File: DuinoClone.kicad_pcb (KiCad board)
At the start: 2 copper layers, 17 parts, among them J1 Digital pins, J2 Serial, J3 ICSP, J4 I2C, U1 DS1337S+, U2 24LC1025, U3 24LC1025, U4 ATMEGA328P-AU, Y1 Crystal 32MHz, Y2 Crystal 16MHz

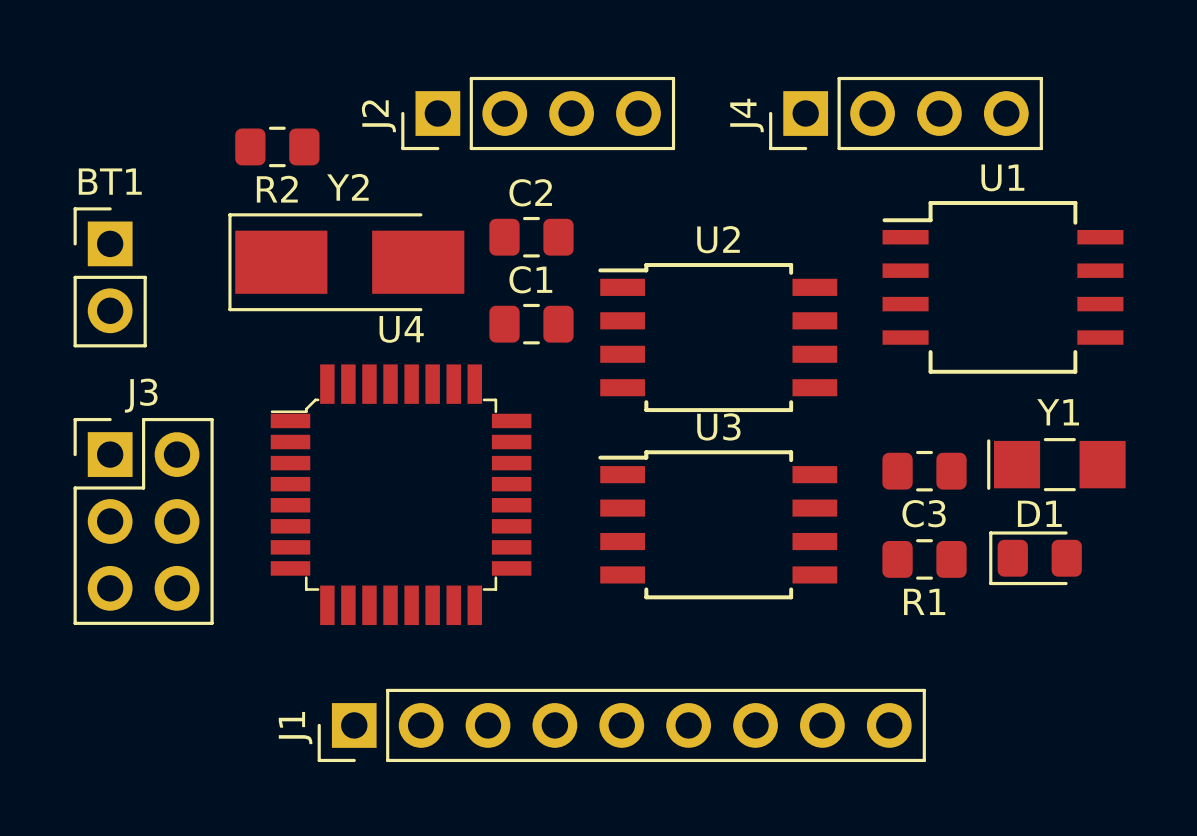
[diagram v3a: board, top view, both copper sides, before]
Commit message: Created PCB outline and drill holes
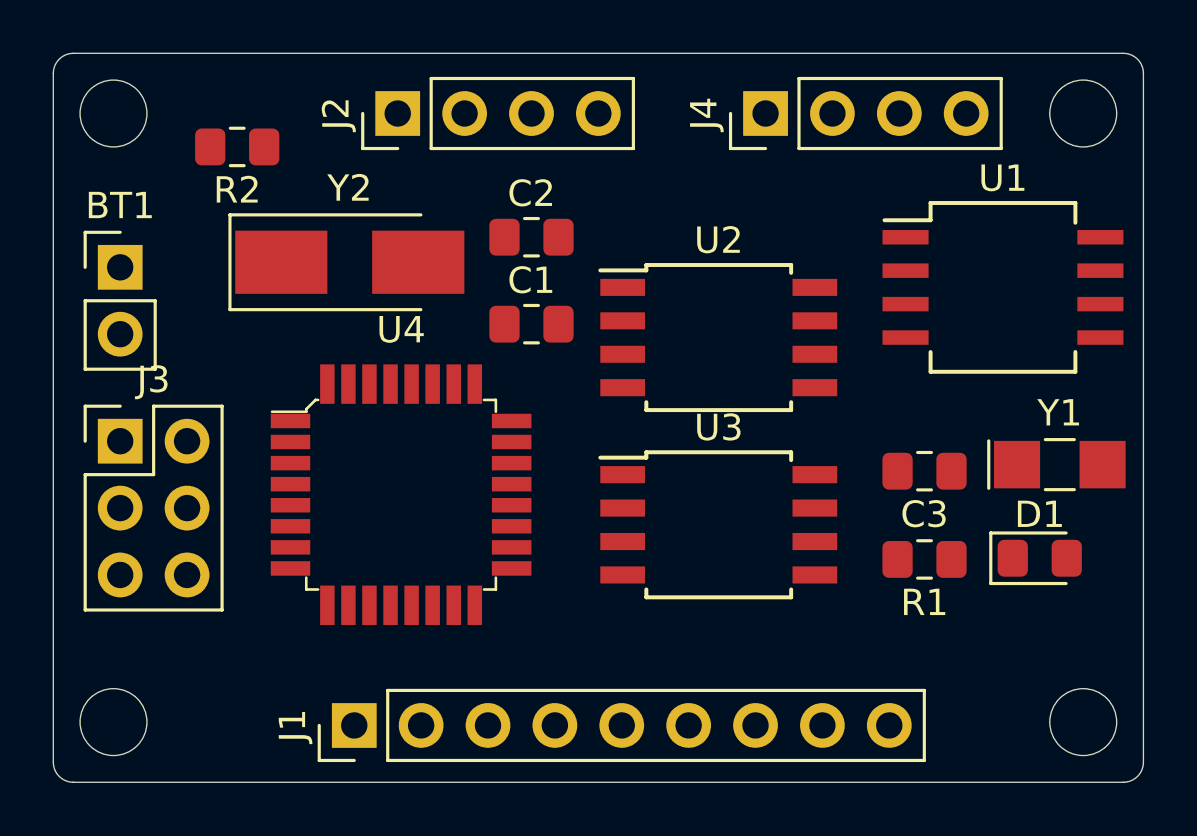
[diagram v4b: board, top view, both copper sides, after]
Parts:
- moved J2 1.52 mm to (93.3, 85.6)
- moved J4 1.52 mm to (107.3, 85.6)
- moved R2 1.52 mm to (87.2, 86.9)
- moved BT1 0.97 mm to (82.8, 91.4)
- moved J3 0.64 mm to (82.8, 98.0)
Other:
- board outline added: 41.4 x 27.7 mm
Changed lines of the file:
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@@
   (general
     (thickness 1.6)
-    (drawings 0)
+    (drawings 12)
     (tracks 0)
     (zones 0)
@@
   )
   (module Connector_PinHeader_2.54mm:PinHeader_1x02_P2.54mm_Vertical (layer F.Cu)
-    (at 82.423 90.551)
+    (at 82.804 91.44)
     (descr "Through hole straight pin header, 1x02, 2.54mm pitch, single row")
     (tags "Through hole pin header THT 1x02 2.54mm single row")
@@
   )
   (module Connector_PinHeader_2.54mm:PinHeader_1x04_P2.54mm_Vertical (layer F.Cu)
-    (at 94.869 85.598 90)
+    (at 93.345 85.598 90)
     (descr "Through hole straight pin header, 1x04, 2.54mm pitch, single row")
     (tags "Through hole pin header THT 1x04 2.54mm single row")
@@
   )
   (module Connector_PinHeader_2.54mm:PinHeader_2x03_P2.54mm_Vertical (layer F.Cu)
-    (at 82.423 98.552)
+    (at 82.804 98.044)
     (descr "Through hole straight pin header, 2x03, 2.54mm pitch, double rows")
     (tags "Through hole pin header THT 2x03 2.54mm double row")
@@
   )
   (module Connector_PinHeader_2.54mm:PinHeader_1x04_P2.54mm_Vertical (layer F.Cu)
-    (at 108.839 85.598 90)
+    (at 107.315 85.598 90)
     (descr "Through hole straight pin header, 1x04, 2.54mm pitch, single row")
     (tags "Through hole pin header THT 1x04 2.54mm single row")
@@
   )
   (module Resistor_SMD:R_0805_2012Metric_Pad1.15x1.40mm_HandSolder (layer F.Cu)
-    (at 88.773 86.868 180)
+    (at 87.249 86.868 180)
     (descr "Resistor SMD 0805 (2012 Metric), square (rectangular) end terminal, IPC_7351 nominal with elongated pad for handsoldering. (Body size source: https://docs.google.com/spreadsheets/d/1BsfQQcO9C6DZCsRaXUlFlo91Tg2WpOkGARC1WS5S8t0/edit?usp=sharing), generated with kicad-footprint-generator")
     (tags "resistor handsolder")
@@
     )
   )
+  (gr_circle (center 119.38 85.598) (end 118.11 85.598) (layer Edge.Cuts) (width 0.05))
+  (gr_circle (center 119.38 108.712) (end 118.11 108.712) (layer Edge.Cuts) (width 0.05))
+  (gr_circle (center 82.55 108.712) (end 81.28 108.712) (layer Edge.Cuts) (width 0.05))
+  (gr_circle (center 82.55 85.598) (end 81.28 85.598) (layer Edge.Cuts) (width 0.05))
+  (gr_line (start 121.666 110.236) (end 121.666 84.074) (layer Edge.Cuts) (width 0.05))
+  (gr_line (start 81.026 110.998) (end 120.904 110.998) (layer Edge.Cuts) (width 0.05))
+  (gr_line (start 80.264 84.074) (end 80.264 110.236) (layer Edge.Cuts) (width 0.05))
+  (gr_line (start 120.904 83.312) (end 81.026 83.312) (layer Edge.Cuts) (width 0.05))
+  (gr_arc (start 120.904 84.074) (end 121.666 84.074) (angle -90) (layer Edge.Cuts) (width 0.05))
+  (gr_arc (start 120.904 110.236) (end 120.904 110.998) (angle -90) (layer Edge.Cuts) (width 0.05))
+  (gr_arc (start 81.026 110.236) (end 80.264 110.236) (angle -90) (layer Edge.Cuts) (width 0.05))
+  (gr_arc (start 81.026 84.074) (end 81.026 83.312) (angle -90) (layer Edge.Cuts) (width 0.05))
 )
